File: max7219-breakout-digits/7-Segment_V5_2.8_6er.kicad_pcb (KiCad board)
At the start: 2 copper layers, 66 x 12 mm, 6 parts, among them J1 Conn_02x08_Odd_Even, U1 7Segment 3 digit CC_STH, U2 7Segment 3 digit CC_STH

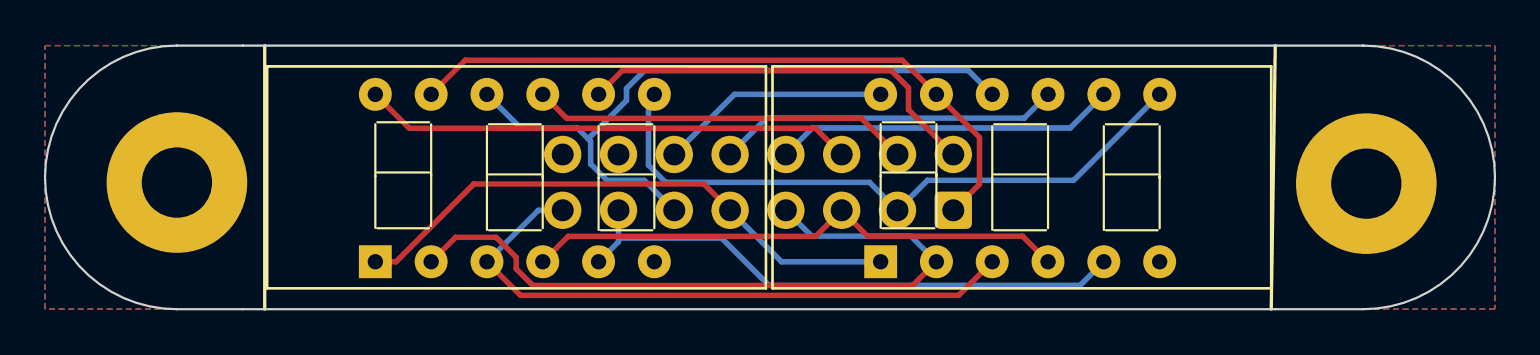
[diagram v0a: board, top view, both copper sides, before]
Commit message: center all mounting holes
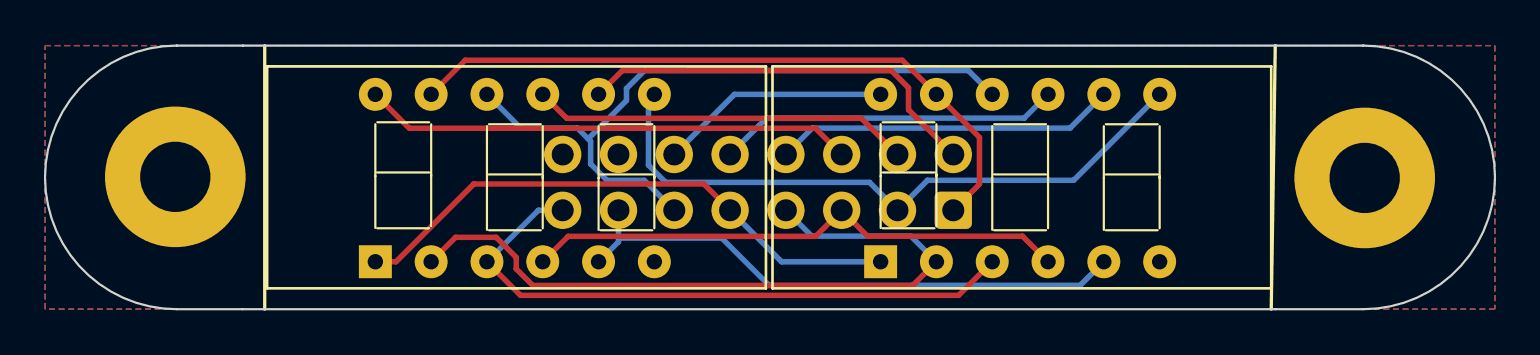
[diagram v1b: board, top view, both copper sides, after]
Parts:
- moved H1 0.27 mm to (64.9, 62.5)
- moved H2 0.27 mm to (119.0, 62.6)
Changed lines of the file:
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@@
 	(footprint "MountingHole:MountingHole_3.2mm_M3_Pad"
 		(layer "F.Cu")
-		(at 64.96 62.79)
+		(at 64.8866 62.5303)
 		(descr "Mounting Hole 3.2mm, M3, generated by kicad-footprint-generator mountinghole.py")
 		(tags "mountinghole M3")
@@
 	(footprint "MountingHole:MountingHole_3.2mm_M3_Pad"
 		(layer "F.Cu")
-		(at 119.1 62.84)
+		(at 119.0266 62.5803)
 		(descr "Mounting Hole 3.2mm, M3, generated by kicad-footprint-generator mountinghole.py")
 		(tags "mountinghole M3")
@@
 			(type solid)
 		)
+		(locked yes)
 		(layer "Edge.Cuts")
 	)
@@
 			(type solid)
 		)
+		(locked yes)
 		(layer "Edge.Cuts")
 	)
@@
 			(type solid)
 		)
+		(locked yes)
 		(layer "Edge.Cuts")
 	)
@@
 			(type solid)
 		)
+		(locked yes)
 		(layer "Edge.Cuts")
 	)
@@
 			(type solid)
 		)
+		(locked yes)
 		(layer "Edge.Cuts")
 	)
@@
 			(type solid)
 		)
+		(locked yes)
 		(layer "Edge.Cuts")
 	)
@@
 			(type solid)
 		)
+		(locked yes)
 		(layer "Edge.Cuts")
 	)
@@
 			(type solid)
 		)
+		(locked yes)
 		(layer "Edge.Cuts")
 	)
@@
 		)
 	)
+	(group ""
+		(members "30c89fb0-d144-491c-8651-f7c9b18de9aa" "41b2a191-795c-4d2e-aa3b-11d277b062b3")
+	)
+	(group ""
+		(locked yes)
+		(members "697bc216-4cd7-4988-9a31-b2a383b793c4" "74d1be10-4b5e-4ee2-9454-d63d3bb89bc5"
+			"78c24942-68bc-409d-bfc7-0165969b3a24" "866aea13-4d1d-40d6-8998-c3ede4eb9696"
+			"a1be515e-a7bb-43c1-b1bb-0aba8f0efd17" "a9cf954d-082c-4fa2-a8f7-0e8b82e95179"
+			"c32ef01f-6cc6-4b1c-b8f1-2a57b102b3c0" "c61cfa6d-b892-47d8-bc1e-f3372fe6c2b6"
+		)
+	)
